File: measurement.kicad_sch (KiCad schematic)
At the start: 16 parts, among them U26001 ACS730xLCTR-20AB, U26002 TLV9352

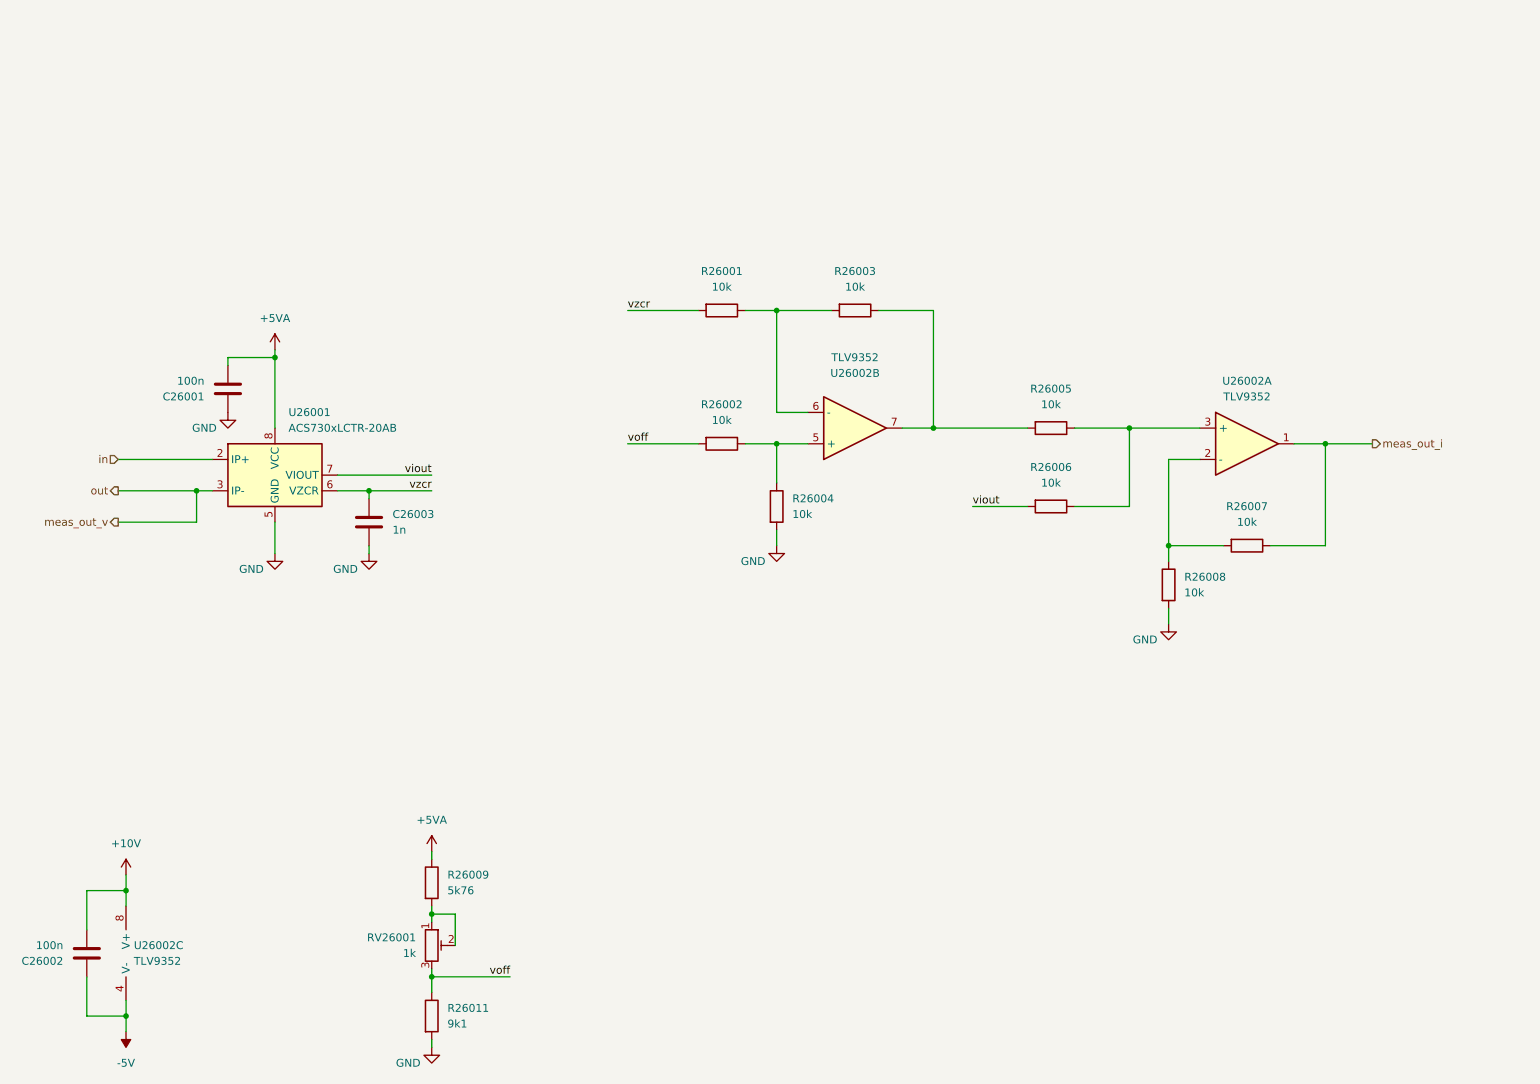
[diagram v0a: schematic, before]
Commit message: edit pss individual power nets for sub circuits
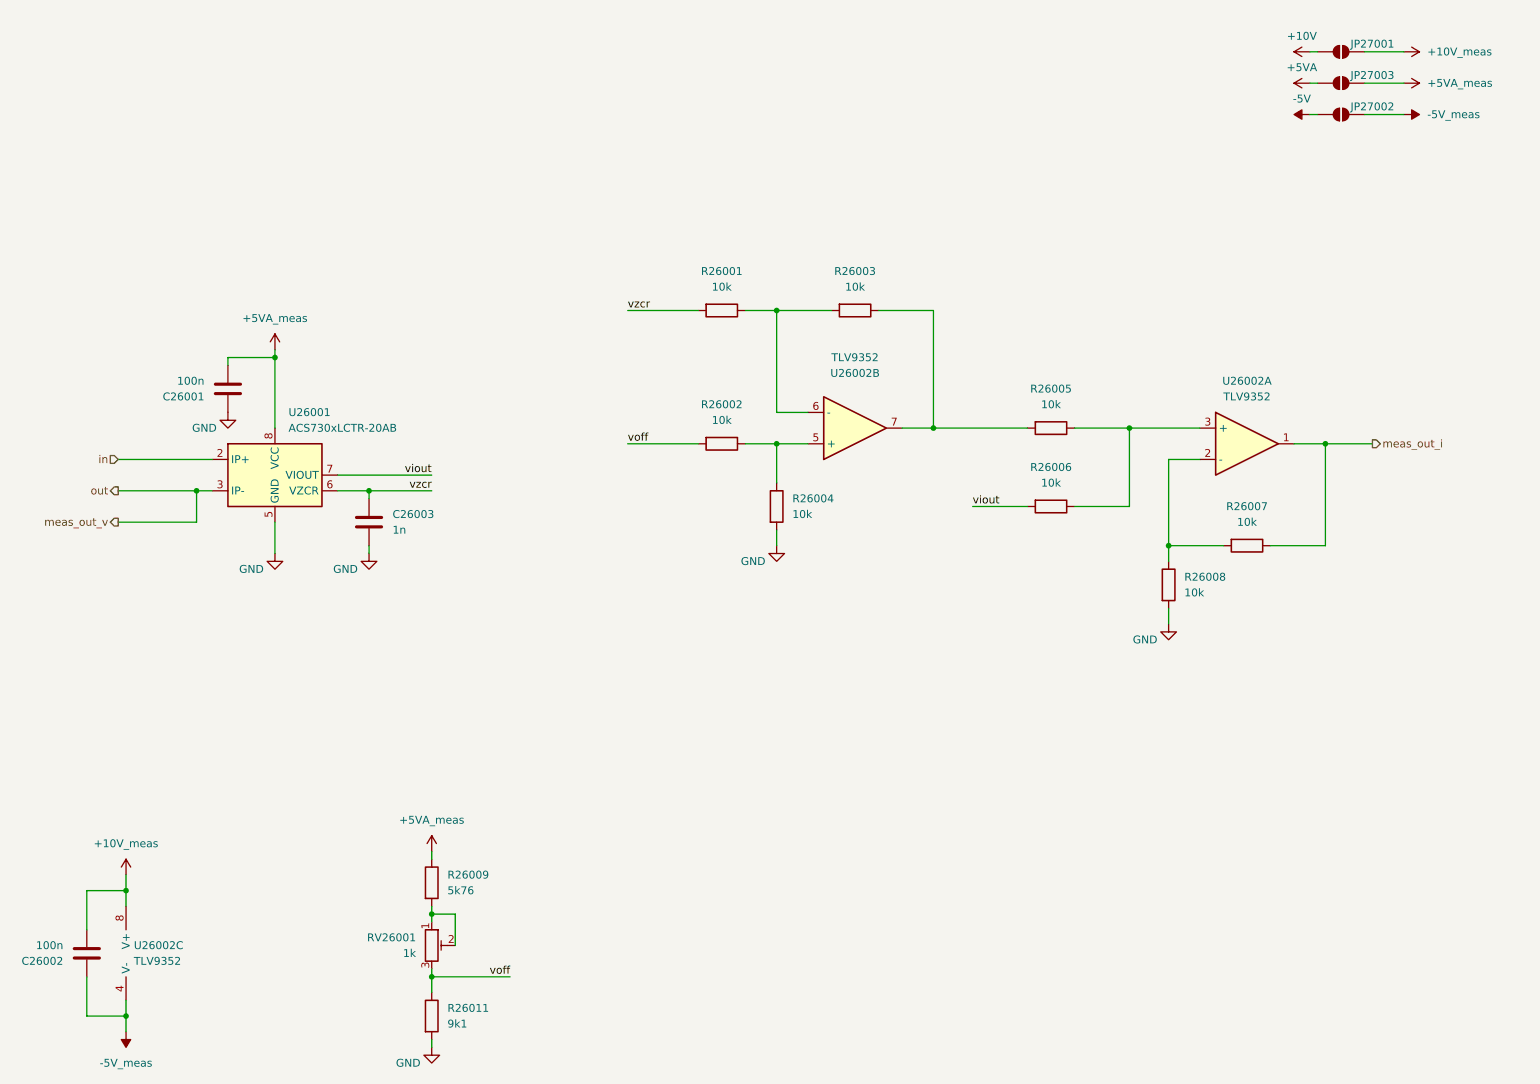
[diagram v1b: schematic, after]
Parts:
- added JP27001, JP27002, JP27003: SolderJumper_2_Open, symbol Jumper:SolderJumper_2_Open
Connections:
- net +10V: now also JP27001.1 (A); no longer C26002.2, U26002.8 (V+)
- net +5VA: now also JP27003.1 (A); no longer C26001.2, R26009.1, U26001.8 (VCC)
- net -5V: now also JP27002.1 (A); no longer C26002.1, U26002.4 (V-)
- new net +10V_meas: C26002.2, JP27001.2 (B), U26002.8 (V+)
- new net +5VA_meas: C26001.2, JP27003.2 (B), R26009.1, U26001.8 (VCC)
- new net -5V_meas: C26002.1, JP27002.2 (B), U26002.4 (V-)

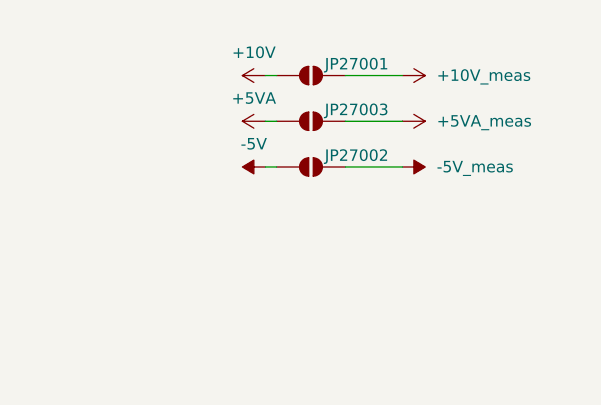
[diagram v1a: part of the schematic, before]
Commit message: fix pss ERC error: missing power flag
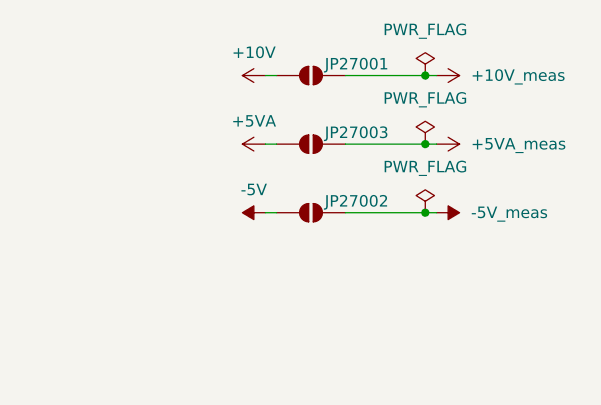
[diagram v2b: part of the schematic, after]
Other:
- moved on the sheet: JP27002, JP27003

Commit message: fix pss ERC errors: multiple outputs connected
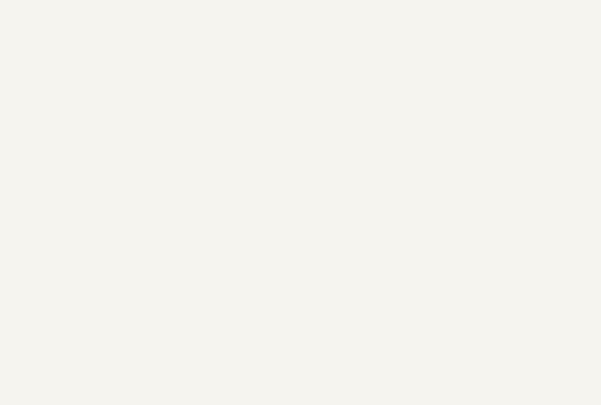
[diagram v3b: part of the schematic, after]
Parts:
- removed JP27001, JP27002, JP27003: SolderJumper_2_Open, symbol Jumper:SolderJumper_2_Open
